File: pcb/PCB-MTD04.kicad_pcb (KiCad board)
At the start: 2 copper layers, 48 parts, among them J1 MotorX, J10 SC_BTNS, J2 Barrel_Jack_Switch, J3 BAU, J4 MotorY, J5 SD, J6 OLED_Screen, J7 SW_XMIN, J8 SW_YMAX, J9 SERVO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

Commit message: uploadPCB
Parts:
- C3, C8, J5, R2, R3: moved to B.Cu
- moved U1 134.8 mm to (165.9, 142.3), turned to -90 degrees
- moved A1 103.5 mm to (157.9, 153.0), turned to 180 degrees
- moved A2 101.2 mm to (135.7, 153.0), turned to 180 degrees
- moved C11 68.7 mm to (157.9, 158.7), turned to 90 degrees
- moved C12 66.2 mm to (161.3, 158.7), turned to 90 degrees
- moved JP6 59.7 mm to (128.8, 125.0)
- moved JP5 59.1 mm to (125.2, 125.0)
- moved J5 59.0 mm to (140.6, 94.8)
- moved JP4 58.6 mm to (121.6, 125.0)
- moved J3 55.9 mm to (164.8, 83.2), turned to 180 degrees
- moved J9 55.1 mm to (148.6, 158.8), turned to 90 degrees
- moved JP1 50.5 mm to (142.3, 125.1)
- moved JP2 50.4 mm to (145.9, 125.1)
- moved JP3 50.4 mm to (149.5, 125.1)
- moved SW1 49.6 mm to (146.4, 82.5)
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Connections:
- A1 pad 1: +3V3 -> GND
- A1 pad 7: +3V3 -> GND
- A2 pad 1: +3V3 -> GND
- A2 pad 7: +3V3 -> GND
- C1 pad 2: +3V3 -> GND
- C10 pad 2: +3V3 -> GND
- C11 pad 2: +3V3 -> GND
- C12 pad 2: +3V3 -> GND
- C13 pad 1: +3V3 -> GND
- C14 pad 2: +3V3 -> GND
- C15 pad 1: +3V3 -> GND
- C16 pad 1: +3V3 -> GND
- C17 pad 1: +3V3 -> GND
- C19 pad 2: +3V3 -> GND
- C3 pad 2: +3V3 -> GND
- C4 pad 2: +3V3 -> GND
- C5 pad 2: +3V3 -> GND
- C6 pad 2: +3V3 -> GND
- C7 pad 2: +3V3 -> GND
- C8 pad 2: +3V3 -> GND
- C9 pad 2: +3V3 -> GND
- D1 pad 1: +3V3 -> GND
- J10 pad 5: +3V3 -> GND
- J2 pad 1: Net-(J3-Pin_1) -> Net-(J3-Pin_2)
- J2 pad 2: +3V3 -> GND
- J2 pad 3: +3V3 -> GND
- J3 pad 1: Net-(J3-Pin_1) -> +12V
- J3 pad 2: +12V -> Net-(J3-Pin_2)
- J5 pad 3: +3V3 -> GND
- J5 pad 6: +3V3 -> GND
- J6 pad 4: +3V3 -> GND
- J7 pad 2: +3V3 -> GND
- J8 pad 2: +3V3 -> GND
- J9 pad 1: +3V3 -> GND
- SW1 pad 1: +3V3 -> GND
- U1 pad 29: +3V3 -> GND
- U1 pad 6: +3V3 -> GND
- U1 pad 7: +3V3 -> GND
- U2 pad 2: +3V3 -> GND
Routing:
- net +3V3: track 0.00 -> 239.8 mm, vias 0 -> 7
- net +12V: track 0.00 -> 136.0 mm
- net +5V: track 0.00 -> 124.6 mm, vias 0 -> 4
- net /Step-X: track 0.00 -> 94.7 mm
- net /BTN_OK: track 0.00 -> 70.3 mm, vias 0 -> 3
- net GND: track 0.00 -> 68.3 mm
- net /Dir-Y: track 0.00 -> 64.3 mm
- net /Step-Y: track 0.00 -> 59.9 mm
- net /Dir-X: track 0.00 -> 57.8 mm, vias 0 -> 4
- net /BTN_DN: track 0.00 -> 53.5 mm
- net /RST: track 0.00 -> 49.7 mm, vias 0 -> 1
- net Net-(J3-Pin_2): track 0.00 -> 47.9 mm
- net /BTN_UP: track 0.00 -> 45.4 mm
- net /CLK: track 0.00 -> 39.8 mm
- net /SERVO_PWM: track 0.00 -> 37.6 mm
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- added copper zone on F.Cu, net GND
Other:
- board outline added: 53.3 x 87.8 mm

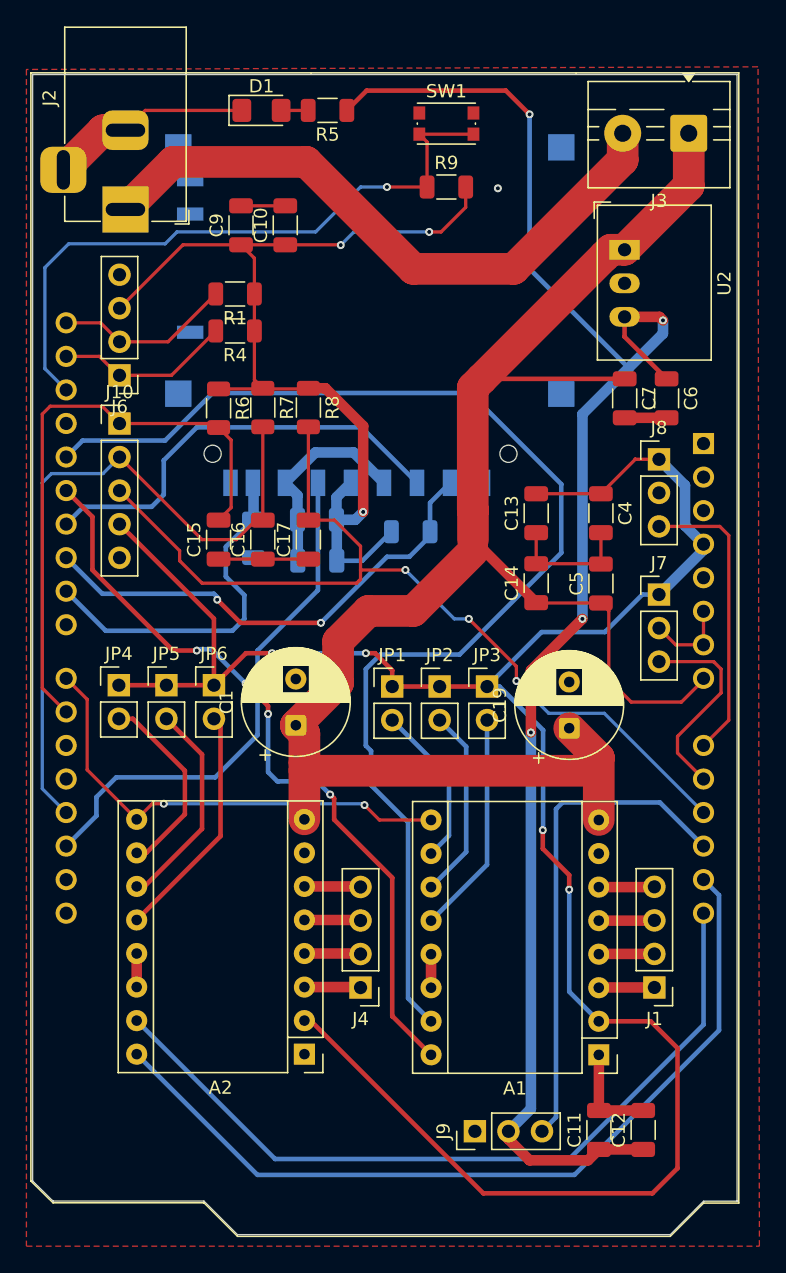
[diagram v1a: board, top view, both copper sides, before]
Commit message: Validation PCB pour production
Attention :
- plan de masse "Front et Bottom"
- Possible collision entre lecteur SD et Barrel Jack Uno
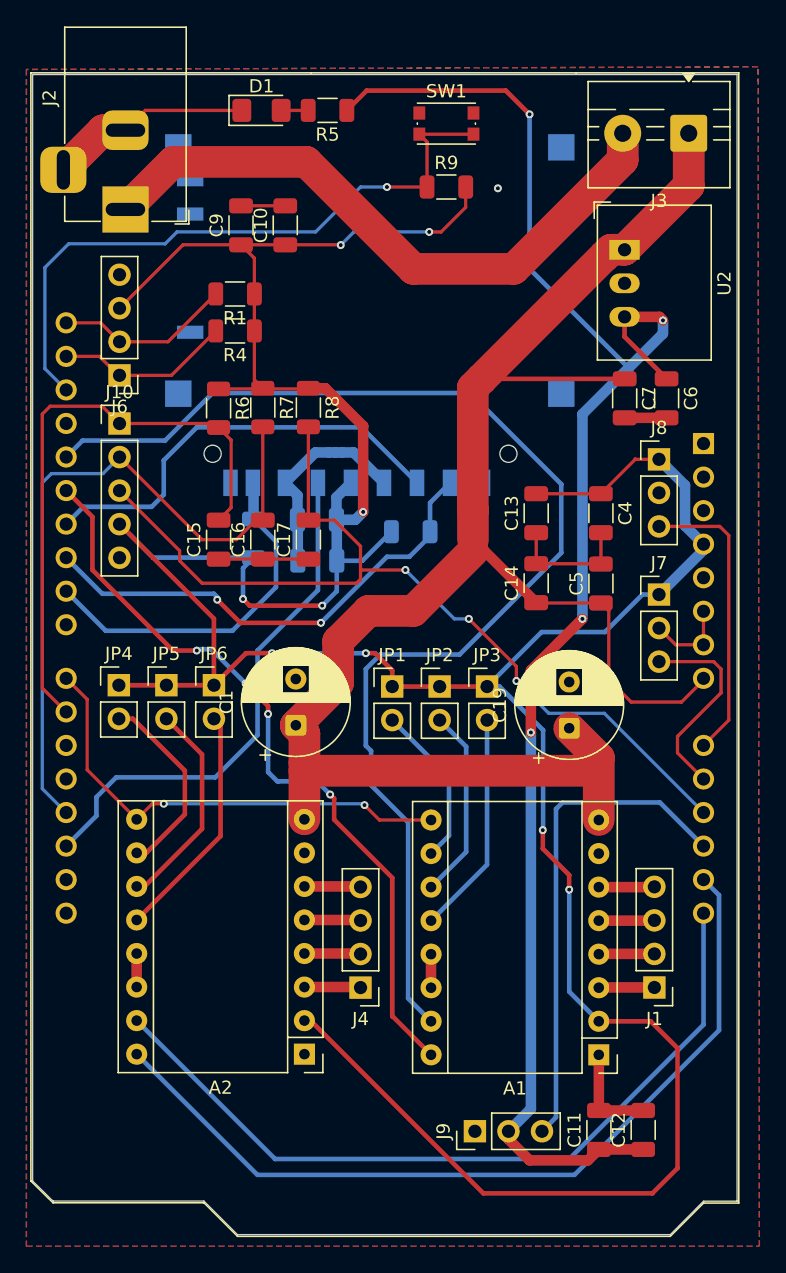
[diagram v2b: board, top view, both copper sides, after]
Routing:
- net +3V3: track 239.8 -> 264.5 mm, vias 7 -> 9
- added copper zone on B.Cu, net GND
